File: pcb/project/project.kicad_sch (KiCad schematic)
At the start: 11 parts, among them J1 Screw_Terminal_01x02, U1 ATmega328-P, U2 LM7805_TO220, Y1 Crystal

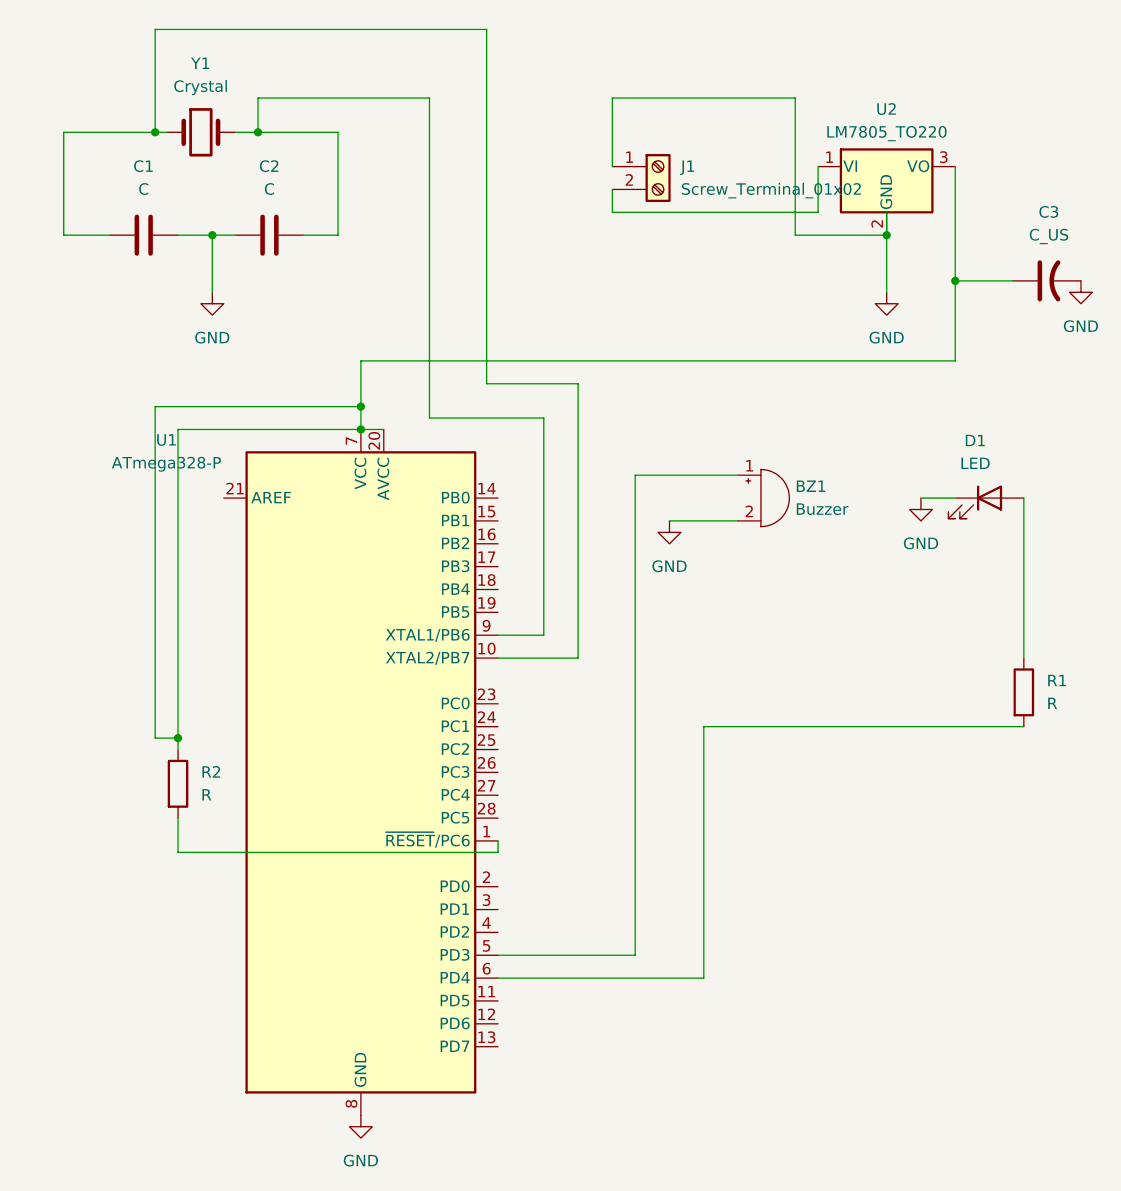
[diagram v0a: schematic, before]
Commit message: fix schematic a bit
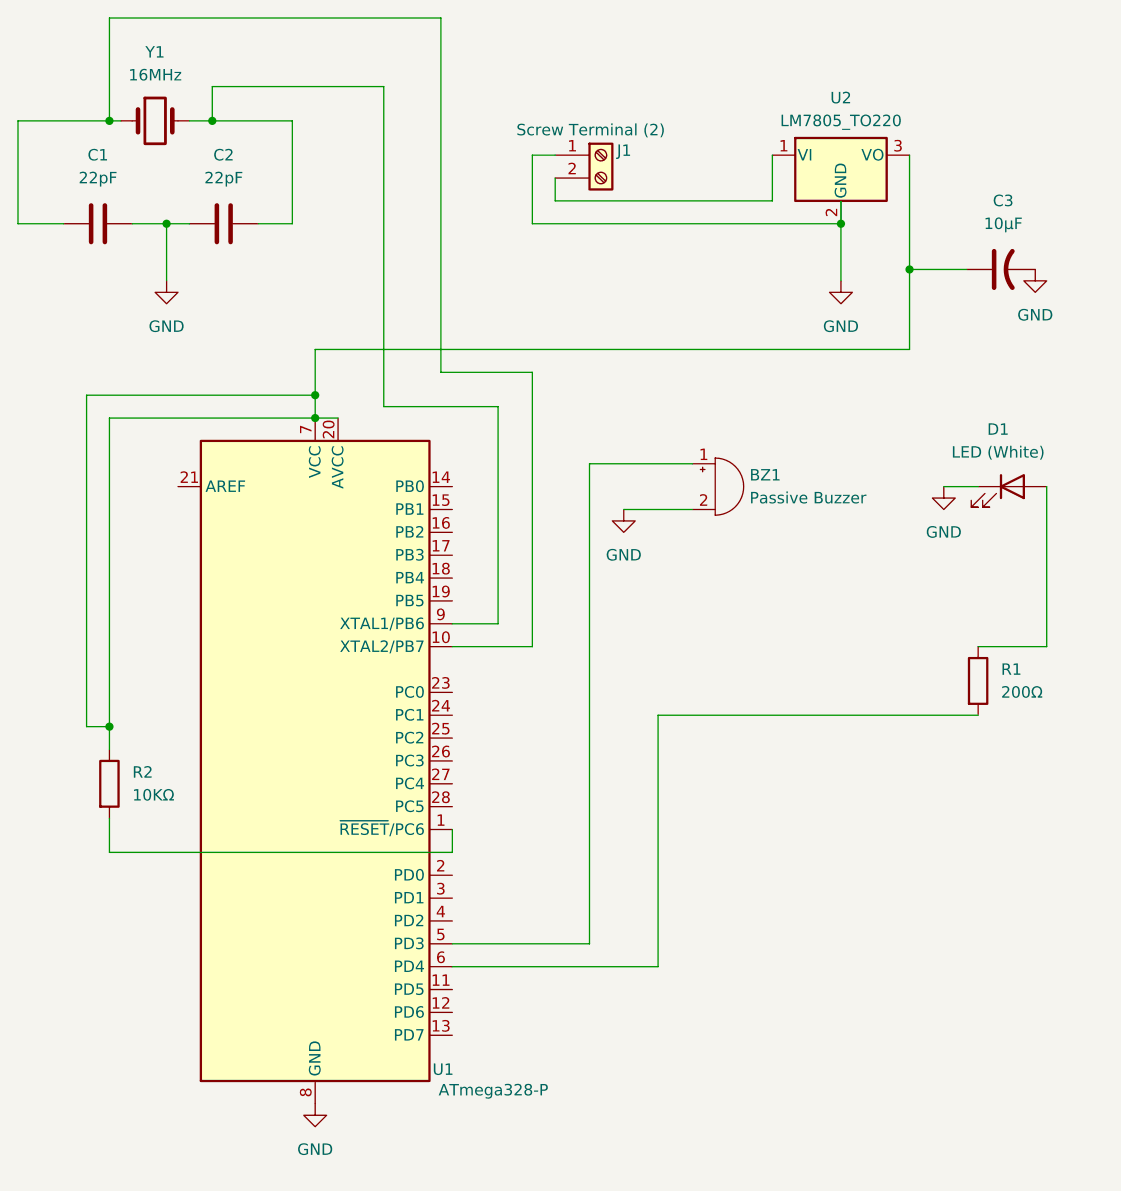
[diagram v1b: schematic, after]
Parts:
- BZ1: value Buzzer -> Passive Buzzer
- C1, C2: value C -> 22pF
- C3: value C_US -> 10μF
- D1: value LED -> LED (White)
- J1: value Screw_Terminal_01x02 -> Screw Terminal (2)
- R1: value R -> 200Ω
- R2: value R -> 10KΩ
- Y1: value Crystal -> 16MHz
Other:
- company: (none) -> KioydioLabs
- title: (none) -> MorseCode Thingy V1
- moved on the sheet: BZ1, C1, C2, C3, D1, J1, R1, R2, U1, U2, Y1
